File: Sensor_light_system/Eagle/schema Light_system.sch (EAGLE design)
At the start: 17 parts, among them IC1 STM32F030C8T6TR, J1 12_WAY_CON

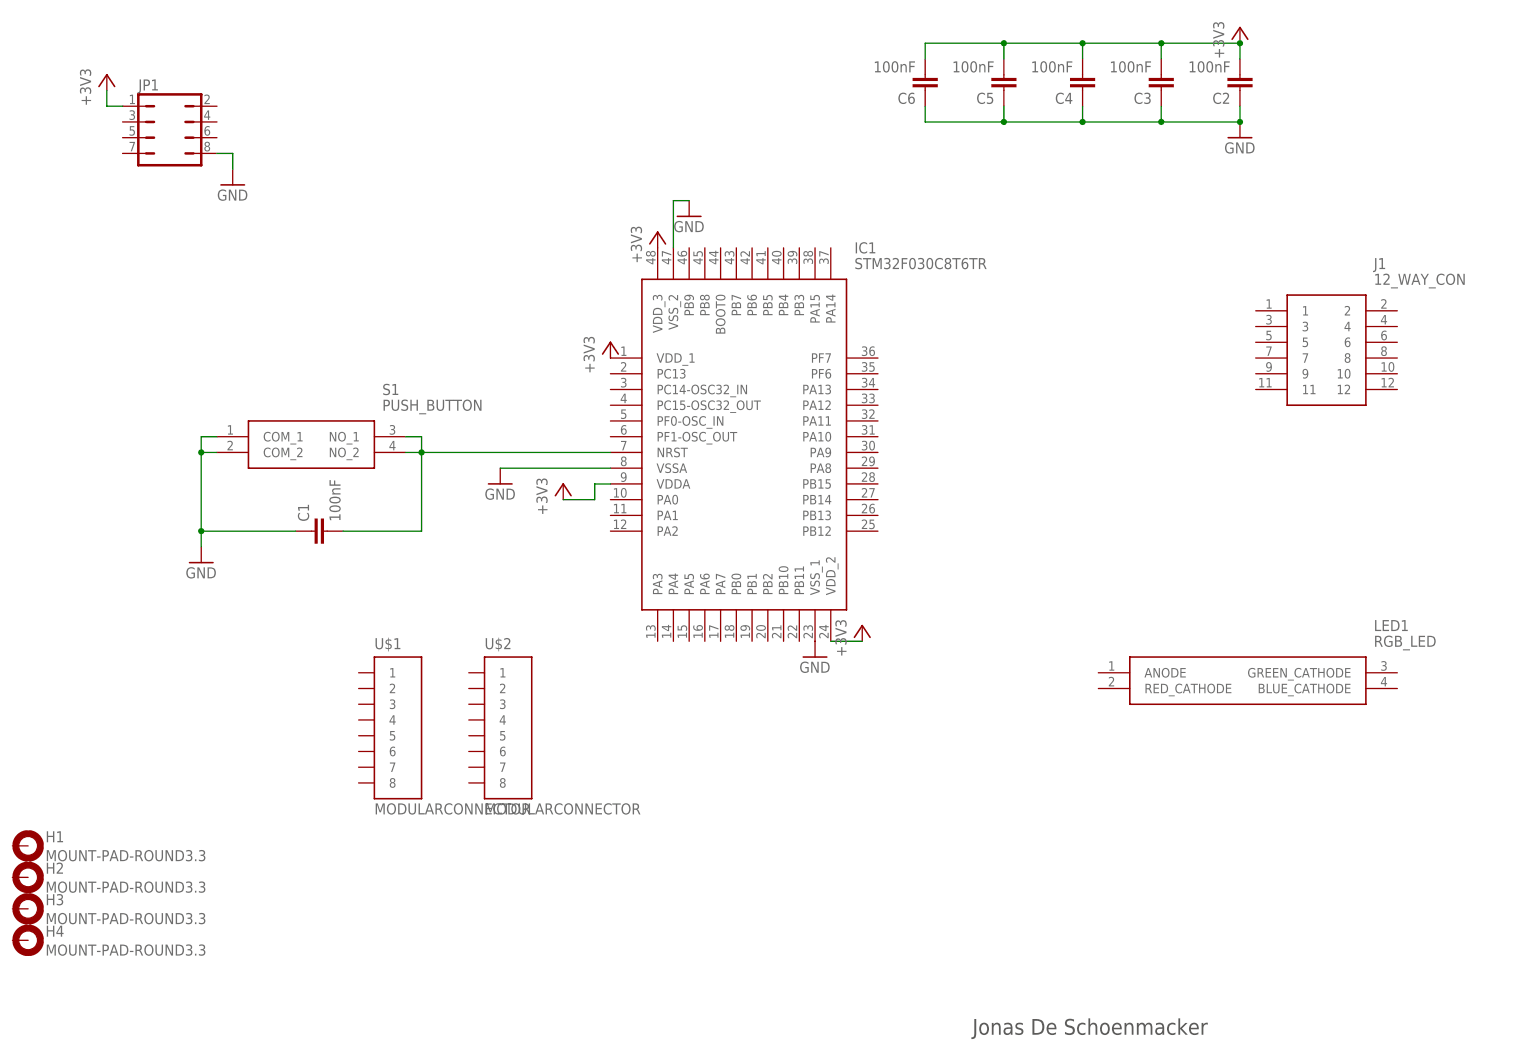
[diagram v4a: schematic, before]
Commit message: schema sensor gewijzigd
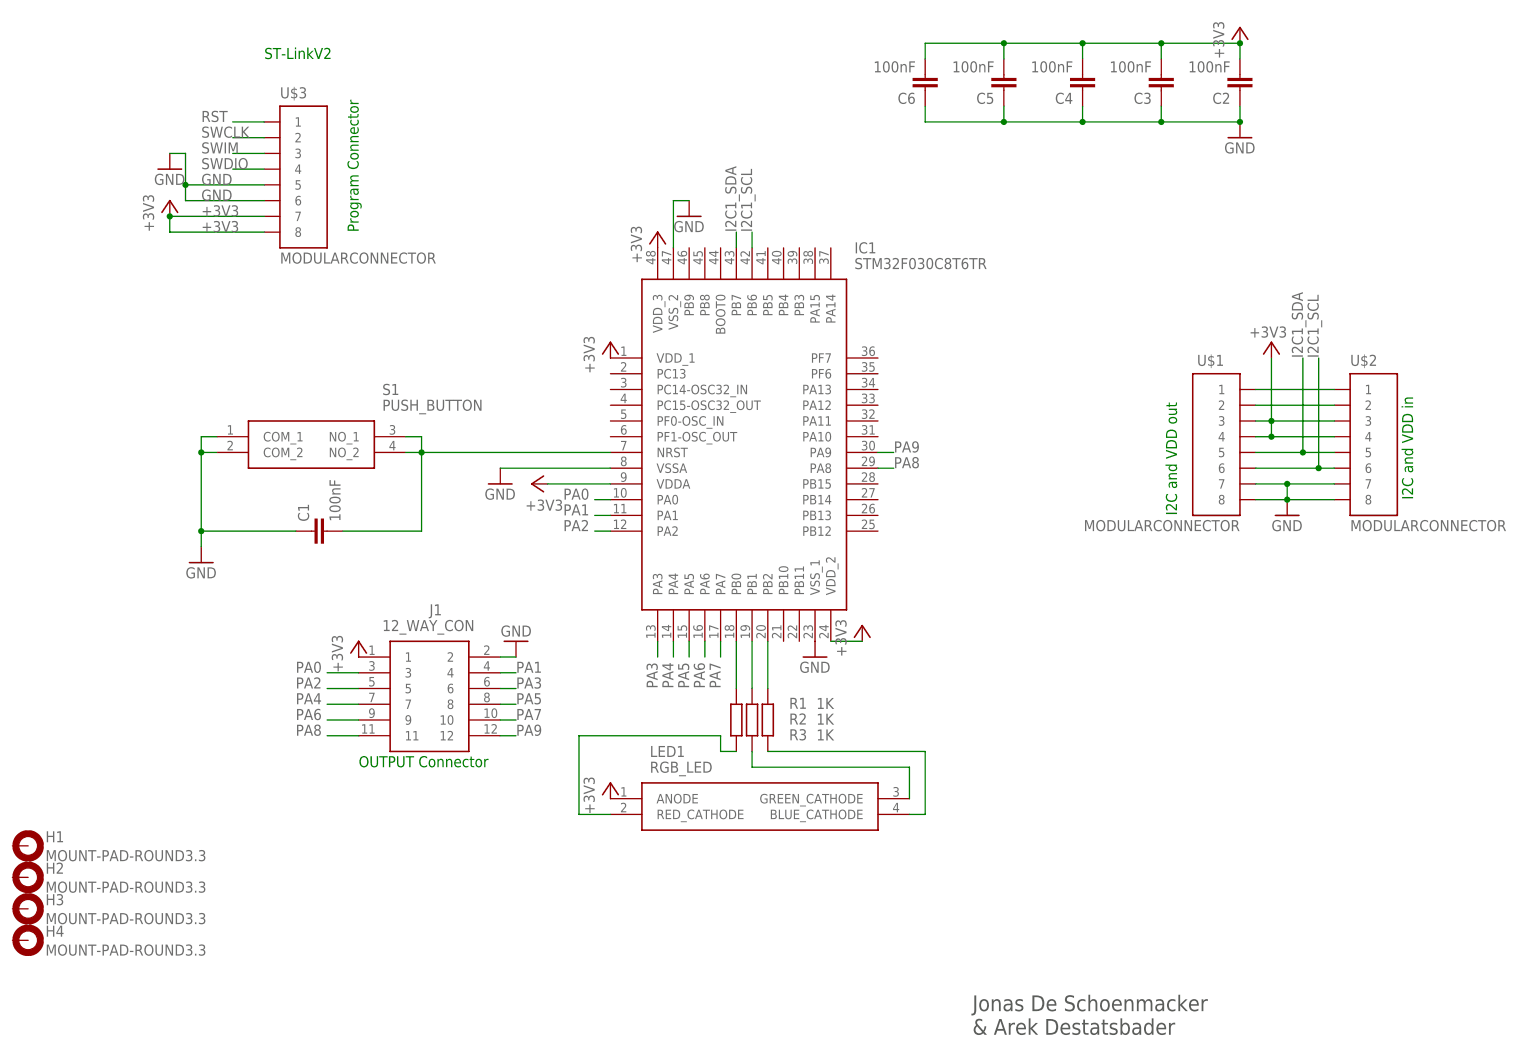
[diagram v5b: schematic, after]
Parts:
- removed JP1: (no value), jumper:JP4Q
- added R1, R2, R3: 1K, rcl:R-EU_R1206
- added U$3: MODULARCONNECTOR, Main_lib:MODULARCONNECTOR
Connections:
- new net I2C1_SCL: IC1.PB6, U$1.6, U$2.6
- new net I2C1_SDA: IC1.PB7, U$1.5, U$2.5
- new net N$2: LED1.GREEN_CATHODE, R1.2, R2.1
- new net N$4: LED1.BLUE_CATHODE, R2.1, R3.1
- new net N$5: R2.2, U$1.1, U$2.1
- new net N$7: IC1.PB1, R2.2
- new net N$8: IC1.PB2, R3.2
- new net PA0: IC1.PA0, J1.3
- new net PA1: IC1.PA1, J1.4
- new net PA2: IC1.PA2, J1.5
- new net PA3: IC1.PA3, J1.6
- new net PA4: IC1.PA4, J1.7
- new net PA5: IC1.PA5, J1.8
- new net PA6: IC1.PA6, J1.9
- new net PA7: IC1.PA7, J1.10
- new net PA8: IC1.PA8, J1.11
- new net PA9: IC1.PA9, J1.12
- new net RST: U$3.1
- new net SWCLK: U$3.2
- new net SWDIO: U$3.4
- new net SWIM: U$3.3
- net +3V3: now also J1.1, LED1.ANODE, R3.2, U$1.3, U$1.4, U$2.3, U$2.4, U$3.7, U$3.8; no longer JP1.1
- net GND: now also J1.2, U$1.7, U$1.8, U$2.7, U$2.8, U$3.5, U$3.6; no longer JP1.5, JP1.8
- net N$1: now also LED1.RED_CATHODE, R1.1; no longer JP1.2
- net N$3: now also R1.1
- net N$6: now also R3.1, U$1.2, U$2.2
- net N$9: now also IC1.PB0, R1.2; no longer JP1.3, JP1.4
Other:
- note added: "I2C and VDD in"
- note added: "I2C and VDD out"
- note added: "Jonas De Schoenmacker & Arek Destatsbader"
- note added: "OUTPUT Connector"
- note added: "Program Connector"
- note added: "Referentie schema"
- note added: "ST-LinkV2"
- moved on the sheet: J1, LED1, U$1, U$2

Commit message: schema Light_system
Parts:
- added C7: 100nF, resistor:C-EUC1206
- added C8: 10nF, resistor:C-EUC1206
- added D1: BAT60J, diode:BAT60J
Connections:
- net +3V3: now also C7.1, C7.2, C8.1, C8.2, D1.A, D1.C
- net GND: now also C7.1, C7.2, C8.1, C8.2
- net N$3: no longer C1.2, IC1.NRST, S1.NO_1, S1.NO_2
- net RST: now also C1.2, IC1.NRST, S1.NO_1, S1.NO_2
- net SWCLK: now also IC1.PA14
- net SWDIO: now also IC1.PA13

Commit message: schema gewijziged
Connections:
- removed net N$3: R1.1
- removed net OSC_IN: C2.2
- removed net OSC_OUT: C1.2
- net +3V3: no longer C4.1, C5.1, C6.1, C7.1, C8.1, R3.2
- net GND: no longer C3.2, C4.2, C5.2, C6.2, C7.2, C8.2, S1.P, S1.P1
- net N$2: no longer R1.2
- net N$4: no longer R2.1
- net N$5: no longer R2.2
- net N$6: no longer C3.1, R3.1, S1.S, S1.S1
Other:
- note removed: "Jonas De Schoenmacker"
- note removed: "Referentie schema"

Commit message: board aangepast
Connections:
- removed net N$6: U$1.2, U$2.2
- net N$5: now also U$1.2, U$2.2
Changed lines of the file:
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@@
 <pinref part="U$2" gate="G$1" pin="1"/>
 <pinref part="U$1" gate="G$1" pin="1"/>
-<wire x1="223.52" y1="111.76" x2="210.82" y2="111.76" width="0.1524" layer="91"/>
+<wire x1="223.52" y1="111.76" x2="215.9" y2="111.76" width="0.1524" layer="91"/>
+<pinref part="U$2" gate="G$1" pin="2"/>
+<pinref part="U$1" gate="G$1" pin="2"/>
+<wire x1="215.9" y1="111.76" x2="210.82" y2="111.76" width="0.1524" layer="91"/>
+<wire x1="223.52" y1="109.22" x2="215.9" y2="109.22" width="0.1524" layer="91"/>
+<wire x1="215.9" y1="109.22" x2="210.82" y2="109.22" width="0.1524" layer="91"/>
+<wire x1="215.9" y1="111.76" x2="215.9" y2="109.22" width="0.1524" layer="91"/>
+<junction x="215.9" y="111.76"/>
+<junction x="215.9" y="109.22"/>
 </segment>
 </net>
-<net name="N$6" class="0">
-<segment>
-<pinref part="U$2" gate="G$1" pin="2"/>
-<pinref part="U$1" gate="G$1" pin="2"/>
-<wire x1="223.52" y1="109.22" x2="210.82" y2="109.22" width="0.1524" layer="91"/>
-</segment>
-</net>
